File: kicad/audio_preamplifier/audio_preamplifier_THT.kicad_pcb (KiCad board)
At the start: 2 copper layers, 34.7 x 26.6 mm, 23 parts, among them P2 CONN_01X03, P3 CONN_01X03, P4 CONN_01X02, U3 TL072

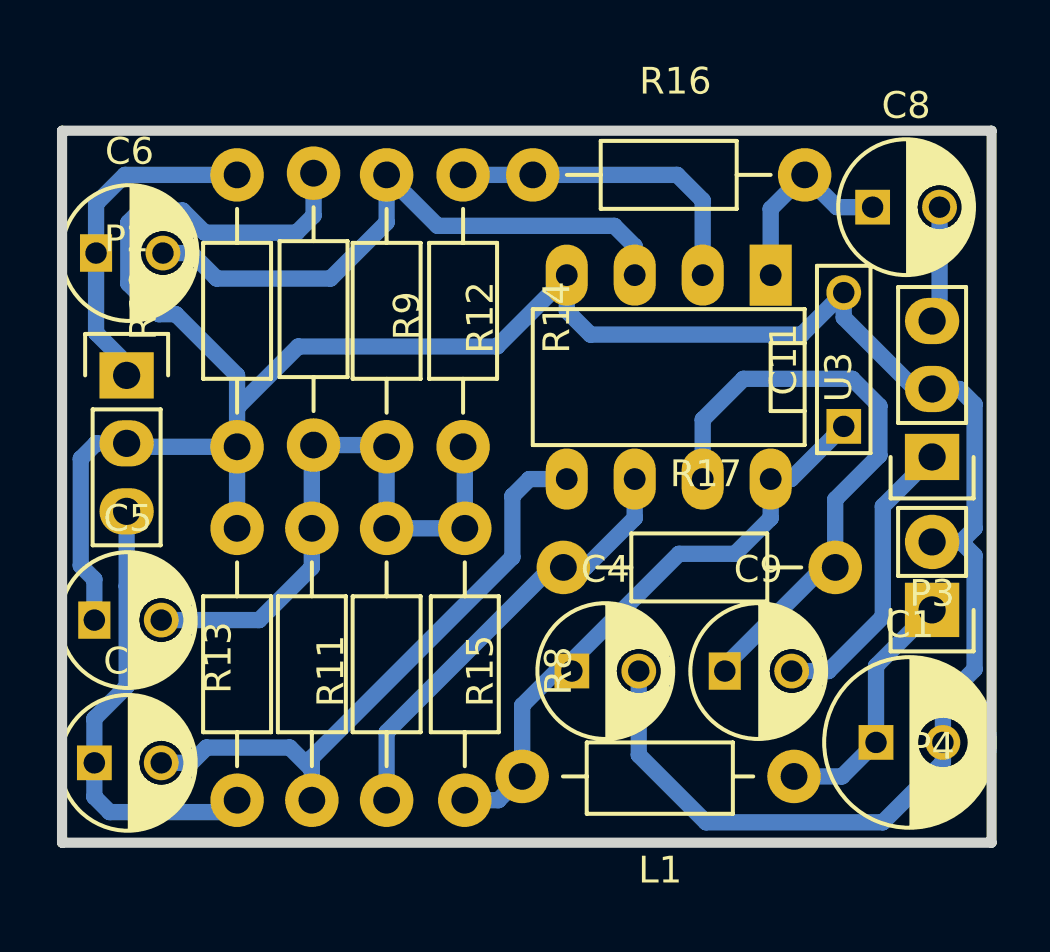
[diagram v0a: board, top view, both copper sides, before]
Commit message: new kicad version components in schematics
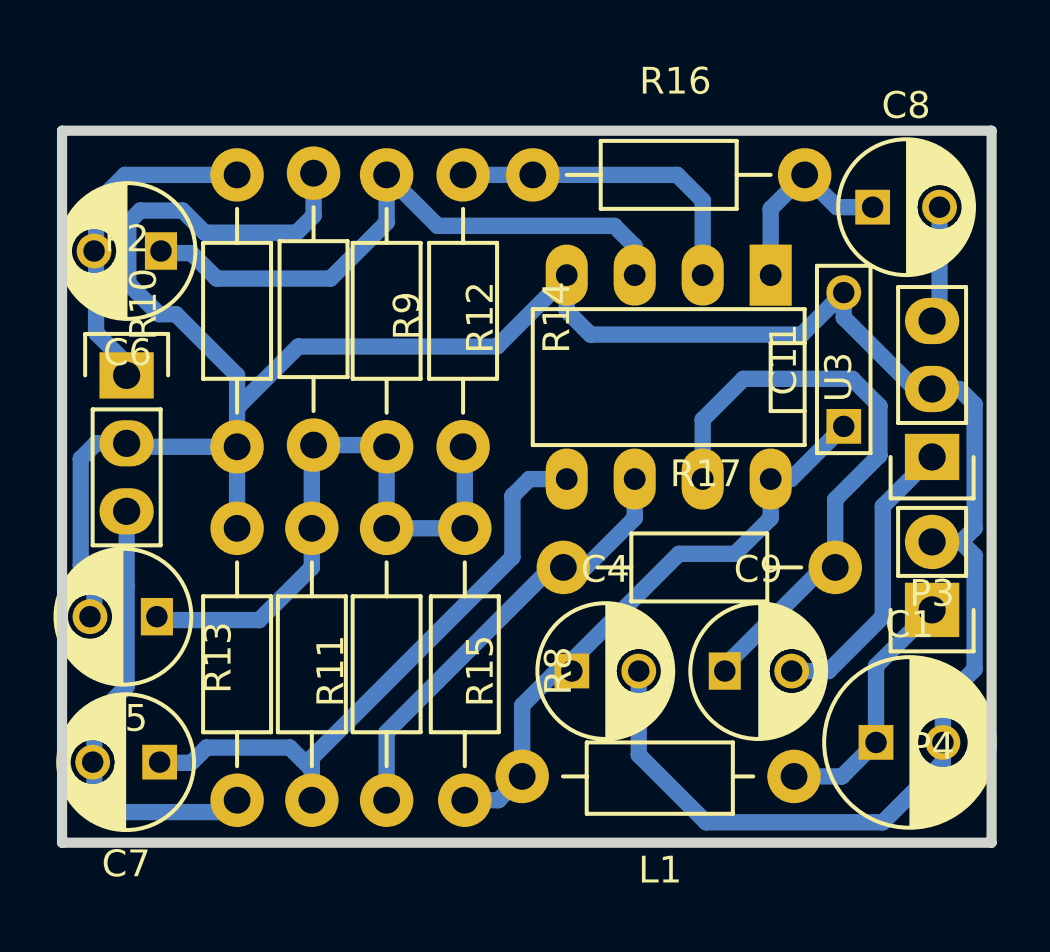
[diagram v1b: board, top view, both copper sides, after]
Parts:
- C1: value 100m -> 100m/25V
- C4, C8, C9: value 47m -> 47m/25V
- C5: value 2m2 -> 2m2/16V
- C6, C7: value 10m -> 10m/16V
- moved C7 2.44 mm to (165.5, 150.0), turned to 180 degrees
- moved C6 2.43 mm to (165.6, 130.9), turned to 180 degrees
- moved C5 2.34 mm to (165.4, 144.5), turned to 180 degrees
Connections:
- C5 pad 1: AGND -> /virtual_gnd
- C5 pad 2: /virtual_gnd -> AGND
- C6 pad 1: right_in -> Net-(C6-Pad1)
- C6 pad 2: Net-(C6-Pad2) -> right_in
- C7 pad 1: left_in -> Net-(C7-Pad1)
- C7 pad 2: Net-(C7-Pad2) -> left_in
- R12 pad 1: Net-(C6-Pad2) -> Net-(C6-Pad1)
- R13 pad 1: Net-(C7-Pad2) -> Net-(C7-Pad1)
- U3 pad 3: Net-(C6-Pad2) -> Net-(C6-Pad1)
- U3 pad 5: Net-(C7-Pad2) -> Net-(C7-Pad1)
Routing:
- net Net-(C7-Pad2): track 23.7 -> 0.00 mm
- net Net-(C7-Pad1): track 0.00 -> 23.7 mm
- net Net-(C6-Pad2): track 23.0 -> 0.00 mm
- net Net-(C6-Pad1): track 0.00 -> 23.0 mm
